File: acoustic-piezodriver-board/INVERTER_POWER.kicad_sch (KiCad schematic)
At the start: 58 parts, among them Q501 AO3400A, Q502 AO3400A, U501 NCE6005AS, U502 LM3478MM, U503 NCE6005AS, U504 LM3478MM

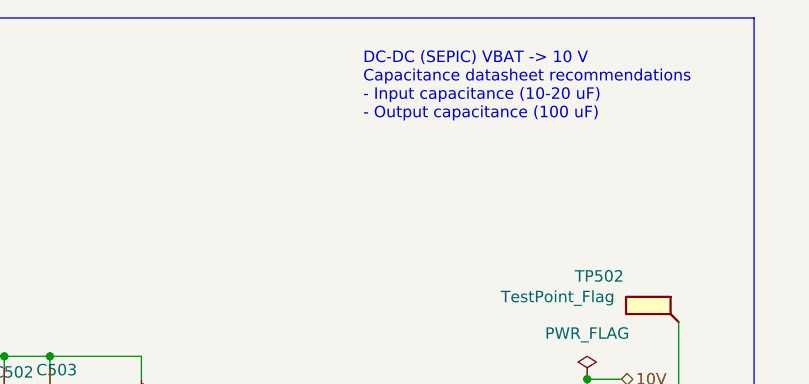
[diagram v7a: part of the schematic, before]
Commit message: rough layout completed, reduce board size and place components accordingly
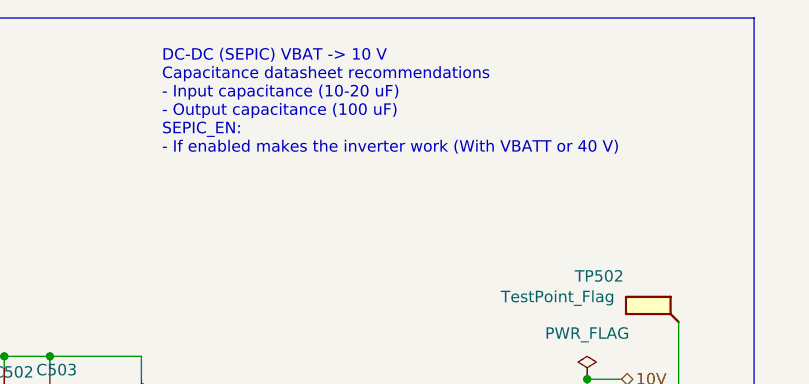
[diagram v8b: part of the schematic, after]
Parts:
- TP501, TP502: footprint TestPoint:TestPoint_THTPad_D2.0mm_Drill1.0mm -> TestPoint:TestPoint_THTPad_D4.0mm_Drill2.0mm
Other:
- note added: "DC-DC (SEPIC) VBAT -> 10 V Capacitance datasheet recommendations - Input capacitance (10-20 uF) - Output capacitance (100 uF) SEPIC_EN: - If enabled makes the inverter work (With VBATT or 40 V)"
- note removed: "DC-DC (SEPIC) VBAT -> 10 V Capacitance datasheet recommendations - Input capacitance (10-20 uF) - Output capacitance (100 uF)"
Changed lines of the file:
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@@
 		)
 	)
-	(text "DC-DC (SEPIC) VBAT -> 10 V\nCapacitance datasheet recommendations\n- Input capacitance (10-20 uF)\n- Output capacitance (100 uF) "
+	(text "DC-DC (SEPIC) VBAT -> 10 V\nCapacitance datasheet recommendations\n- Input capacitance (10-20 uF)\n- Output capacitance (100 uF) \nSEPIC_EN:\n- If enabled makes the inverter work (With VBATT or 40 V)"
 		(exclude_from_sim no)
-		(at 349.758 28.448 0)
+		(at 327.406 30.226 0)
 		(effects
 			(font
@@
 			)
 		)
-		(property "Footprint" "TestPoint:TestPoint_THTPad_D2.0mm_Drill1.0mm"
+		(property "Footprint" "TestPoint:TestPoint_THTPad_D4.0mm_Drill2.0mm"
 			(at 379.73 54.61 0)
 			(effects
@@
 			)
 		)
-		(property "Footprint" "TestPoint:TestPoint_THTPad_D2.0mm_Drill1.0mm"
+		(property "Footprint" "TestPoint:TestPoint_THTPad_D4.0mm_Drill2.0mm"
 			(at 359.41 185.42 0)
 			(effects
